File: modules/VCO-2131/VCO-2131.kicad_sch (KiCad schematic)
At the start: 51 parts, among them U4 SSI2131, U5 TL074, U6 TL074, U7 TL074, U8 SN74HCS74

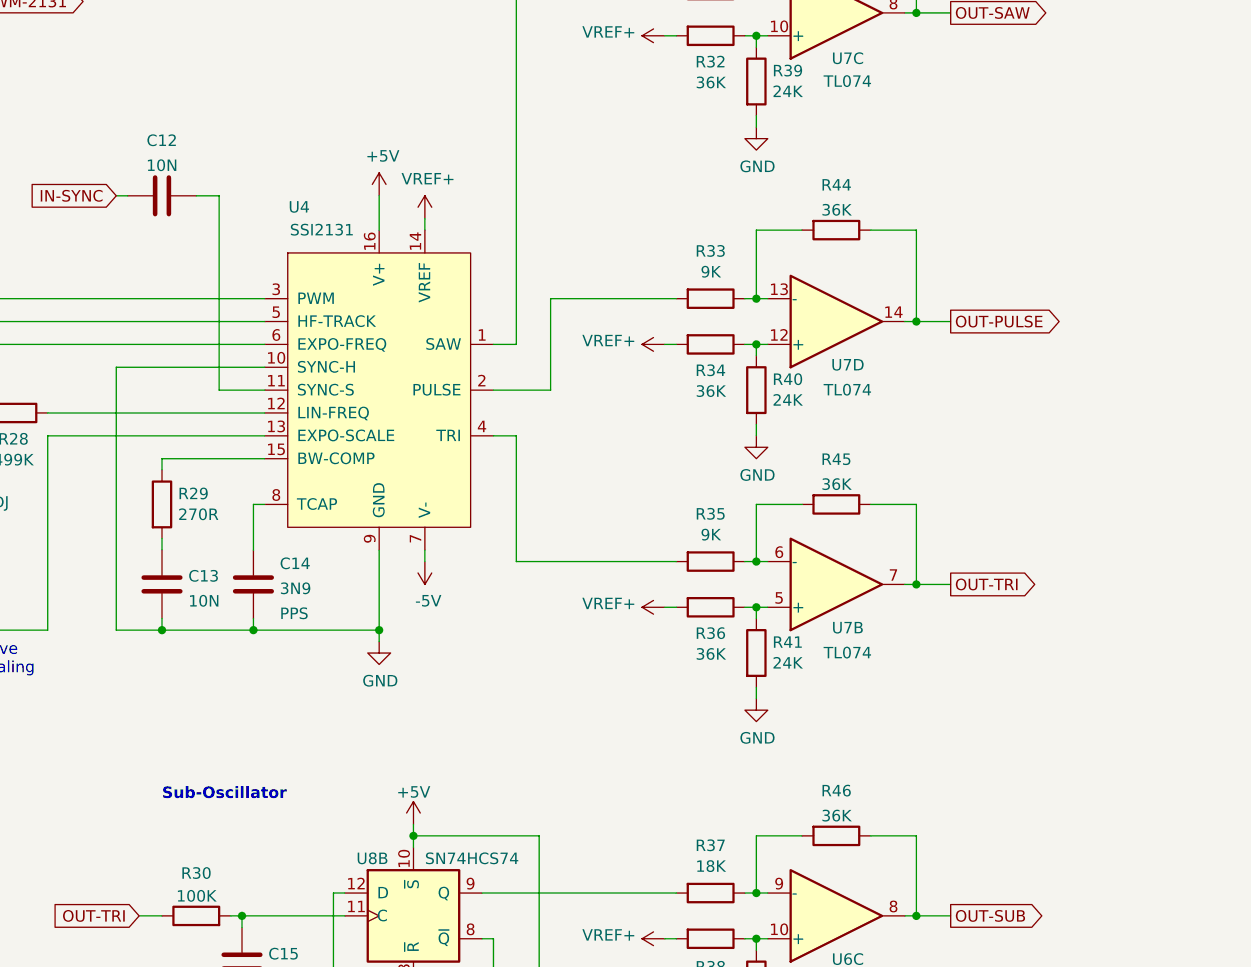
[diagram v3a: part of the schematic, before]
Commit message: VCO sub fix - schematic & PCB cleanup
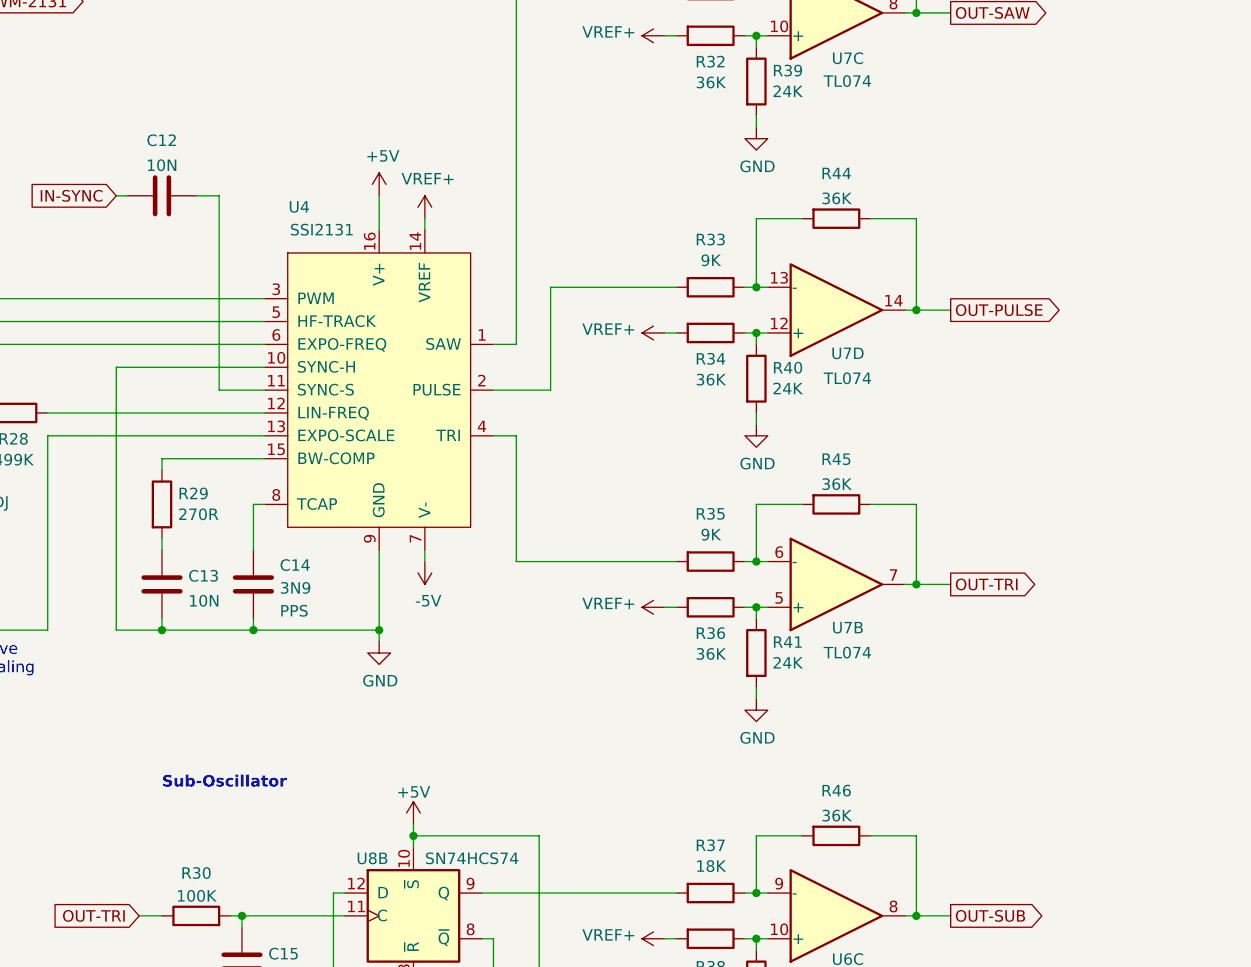
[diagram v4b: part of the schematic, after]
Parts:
- C14: Note PPS -> (none); Value2 (none) -> PPS
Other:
- moved on the sheet: R33, R34, R40, R44, U7D

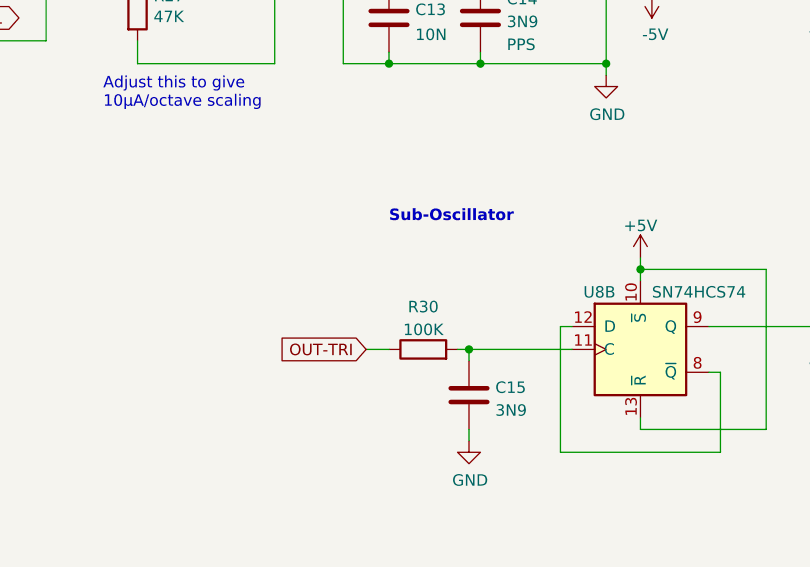
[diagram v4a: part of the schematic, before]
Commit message: VCO sub fix - TODOs
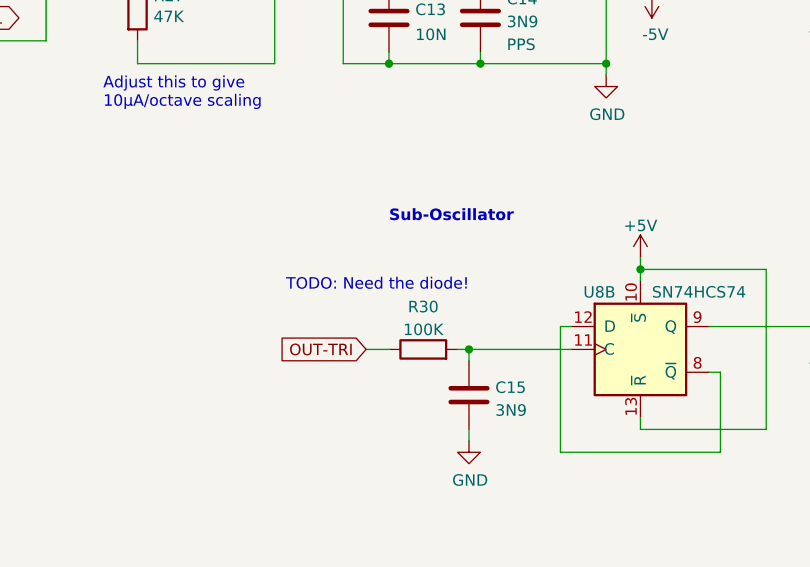
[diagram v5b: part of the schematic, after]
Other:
- note added: "TODO: Need the diode!"
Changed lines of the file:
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@@
     (effects (font (size 1.27 1.27) (thickness 0.254) bold) (justify left bottom))
+  )
+  (text "TODO: Need the diode!" (at 142.24 130.81 0)
+    (effects (font (size 1.27 1.27)) (justify left bottom))
   )
   (text "PWM CV: -5V to +5V\nPW Pot: +5V to -5V" (at 20.32 46.99 0)

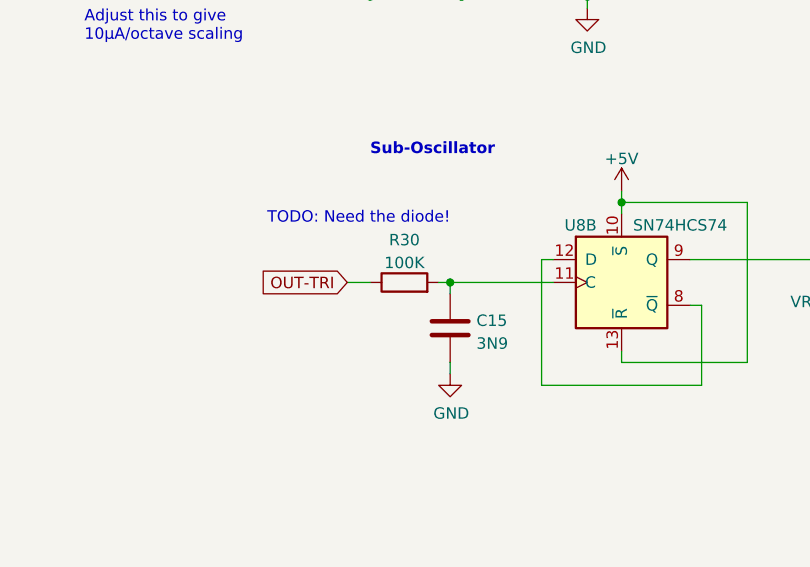
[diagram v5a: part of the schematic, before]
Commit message: VCO sub fix - main module design updated
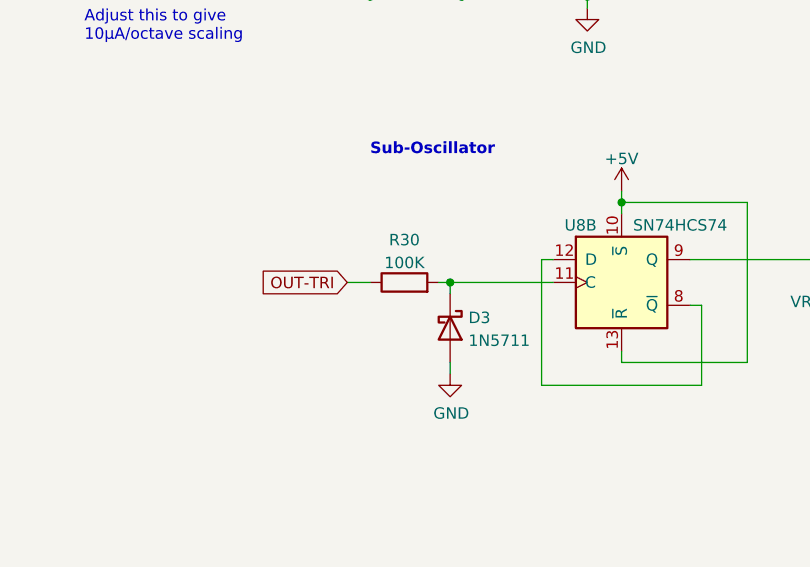
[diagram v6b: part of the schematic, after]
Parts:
- removed C15: 3N9, -lmp-misc:C_Rect_Kemet_L7.2mm_W2.5mm_P5mm, symbol -lmp:CC
- added D3: 1N5711, Diode_THT:D_DO-35_SOD27_P7.62mm_Horizontal, symbol -lmp-diode:1N5711
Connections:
- net GND: now also D3.2 (A)
- net at R30.2, U8.11 (C): now also D3.1 (K)
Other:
- note removed: "TODO: Need the diode!"
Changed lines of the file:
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@@
     (effects (font (size 1.27 1.27) (thickness 0.254) bold) (justify left bottom))
-  )
-  (text "TODO: Need the diode!" (at 142.24 130.81 0)
-    (effects (font (size 1.27 1.27)) (justify left bottom))
   )
   (text "PWM CV: -5V to +5V\nPW Pot: +5V to -5V" (at 20.32 46.99 0)
@@
     (pin "2")
   )
+  (symbol (lib_id "-lmp-diode:1N5711") (at 162.56 142.24 270) (unit 1)
+    (in_bom yes) (on_board yes) (fields_autoplaced)
+    (property "Reference" "D3" (id 0) (at 164.592 141.0878 90)
+      (effects (font (size 1.27 1.27)) (justify left))
+    )
+    (property "Value" "1N5711" (id 1) (at 164.592 143.6247 90)
+      (effects (font (size 1.27 1.27)) (justify left))
+    )
+    (property "Footprint" "Diode_THT:D_DO-35_SOD27_P7.62mm_Horizontal" (id 2) (at 162.56 142.24 0)
+      (effects (font (size 1.27 1.27)) hide)
+    )
+    (property "Datasheet" "https://www.mouser.ca/datasheet/2/389/cd00000759-1795802.pdf" (id 3) (at 162.56 142.24 0)
+      (effects (font (size 1.27 1.27)) hide)
+    )
+    (property "Manufacturer" "STMicroelectronics" (id 4) (at 162.56 142.24 0)
+      (effects (font (size 1.27 1.27)) hide)
+    )
+    (property "ManufacturerPartNum" "1N5711" (id 5) (at 162.56 142.24 0)
+      (effects (font (size 1.27 1.27)) hide)
+    )
+    (property "Distributor" "Mouser" (id 6) (at 162.56 142.24 0)
+      (effects (font (size 1.27 1.27)) hide)
+    )
+    (property "DistributorPartNum" "511-1N5711" (id 7) (at 162.56 142.24 0)
+      (effects (font (size 1.27 1.27)) hide)
+    )
+    (property "DistributorPartLink" "https://www.mouser.ca/ProductDetail/STMicroelectronics/1N5711?qs=FITO%2F%2FQgYDnH7pJ7rS2FRA%3D%3D" (id 8) (at 162.56 142.24 0)
+      (effects (font (size 1.27 1.27)) hide)
+    )
+    (pin "1")
+    (pin "2")
+  )
   (symbol (lib_name "R_1%_0W166_25") (lib_id "-lmp:R_1%_0W166") (at 219.71 77.47 0) (unit 1)
     (in_bom yes) (on_board yes)
@@
     (pin "2")
   )
-  (symbol (lib_id "-lmp:CC") (at 162.56 142.24 0) (unit 1)
-    (in_bom yes) (on_board yes) (fields_autoplaced)
-    (property "Reference" "C15" (id 0) (at 165.481 141.4053 0)
-      (effects (font (size 1.27 1.27)) (justify left))
-    )
-    (property "Value" "3N9" (id 1) (at 165.481 143.9422 0)
-      (effects (font (size 1.27 1.27)) (justify left))
-    )
-    (property "Footprint" "-lmp-misc:C_Rect_Kemet_L7.2mm_W2.5mm_P5mm" (id 2) (at 163.5252 146.05 0)
-      (effects (font (size 1.27 1.27)) hide)
-    )
-    (property "Datasheet" "https://www.mouser.ca/datasheet/2/281/RDE_C0G_50V_100V_E-1670911.pdf" (id 3) (at 162.56 142.24 0)
-      (effects (font (size 1.27 1.27)) hide)
-    )
-    (property "Manufacturer" "Murata" (id 4) (at 162.56 142.24 0)
-      (effects (font (size 1.27 1.27)) hide)
-    )
-    (property "ManufacturerPartNum" "RDE5C1H392J0K1H03B" (id 5) (at 162.56 142.24 0)
-      (effects (font (size 1.27 1.27)) hide)
-    )
-    (property "Distributor" "Mouser" (id 6) (at 162.56 142.24 0)
-      (effects (font (size 1.27 1.27)) hide)
-    )
-    (property "DistributorPartNum" "81-RDE5C1H392J0K1H3B" (id 7) (at 162.56 142.24 0)
-      (effects (font (size 1.27 1.27)) hide)
-    )
-    (property "DistributorPartLink" "https://www.mouser.ca/ProductDetail/Murata-Electronics/RDE5C1H392J0K1H03B?qs=IAJIiSVA5G9ACJO7FVgavQ%3D%3D" (id 8) (at 162.56 142.24 0)
-      (effects (font (size 1.27 1.27)) hide)
-    )
-    (property "Note" "C15 may be same as C14, or ceramic" (id 9) (at 162.56 142.24 0)
-      (effects (font (size 1.27 1.27)) hide)
-    )
-    (pin "1")
-    (pin "2")
-  )
   (symbol (lib_name "R_1%_0W166_18") (lib_id "-lmp:R_1%_0W166") (at 228.6 26.67 270) (unit 1)
     (in_bom yes) (on_board yes) (fields_autoplaced)
@@
       (reference "C14") (unit 1) (value "3N9") (footprint "-lmp-misc:C_Rect_Kemet_L7.2mm_W2.5mm_P5mm")
     )
-    (path "/fc42b60c-65a0-4d60-9163-ea2425051874"
-      (reference "C15") (unit 1) (value "3N9") (footprint "-lmp-misc:C_Rect_Kemet_L7.2mm_W2.5mm_P5mm")
-    )
     (path "/00000000-0000-0000-0000-000061bb8251"
       (reference "D1") (unit 1) (value "1N5711") (footprint "Diode_THT:D_DO-35_SOD27_P7.62mm_Horizontal")
@@
       (reference "D2") (unit 1) (value "1N5711") (footprint "Diode_THT:D_DO-35_SOD27_P7.62mm_Horizontal")
     )
+    (path "/2d0f224a-0239-4b15-a4e4-6c6835f4f086"
+      (reference "D3") (unit 1) (value "1N5711") (footprint "Diode_THT:D_DO-35_SOD27_P7.62mm_Horizontal")
+    )
     (path "/5591601a-0208-417f-b6e4-bd68e0c1316e/0133c837-7e0d-48bb-b2a7-f840ed9692e9"
